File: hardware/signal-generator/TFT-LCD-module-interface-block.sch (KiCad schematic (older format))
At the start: 6 parts, among them J11 SD_Card_Conn, J12 TP_Conn, J13 LCD_Conn, U22 MCP4551-103E/MS

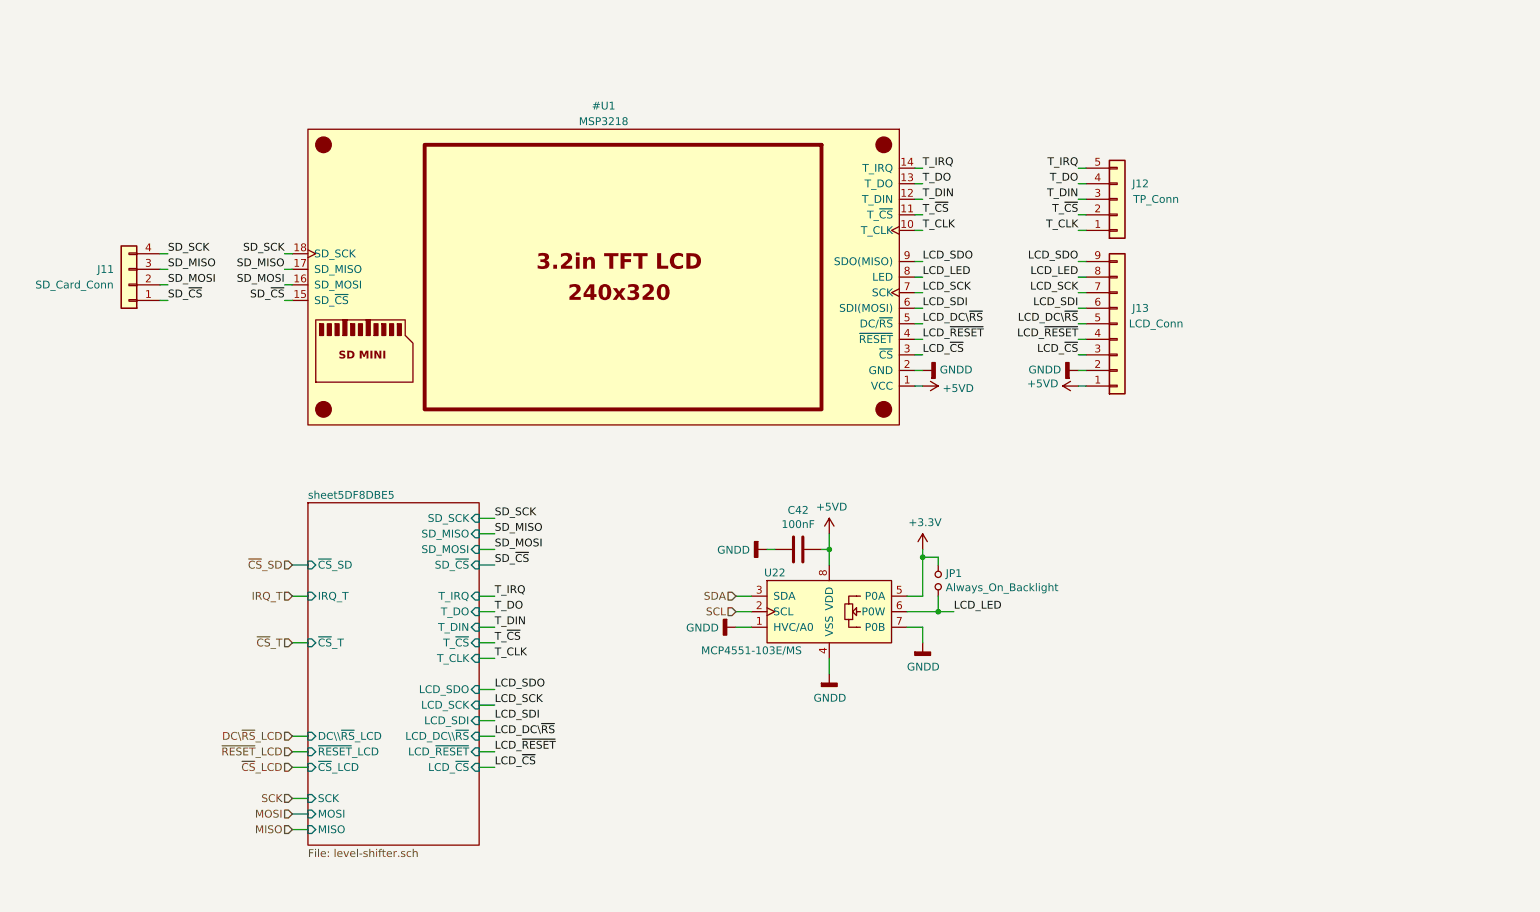
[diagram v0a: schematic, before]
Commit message: [Signal Generator] Change LCD backlight control method
The LCD's backlight was previously intended to be controlled via a
digital potentiometer. However, a much more elegant solution is to
control said backlight via PWM.

Also, removed the level shifter schematic sheet. The level shifters have been
moved to the TFT module's schematic sheet.
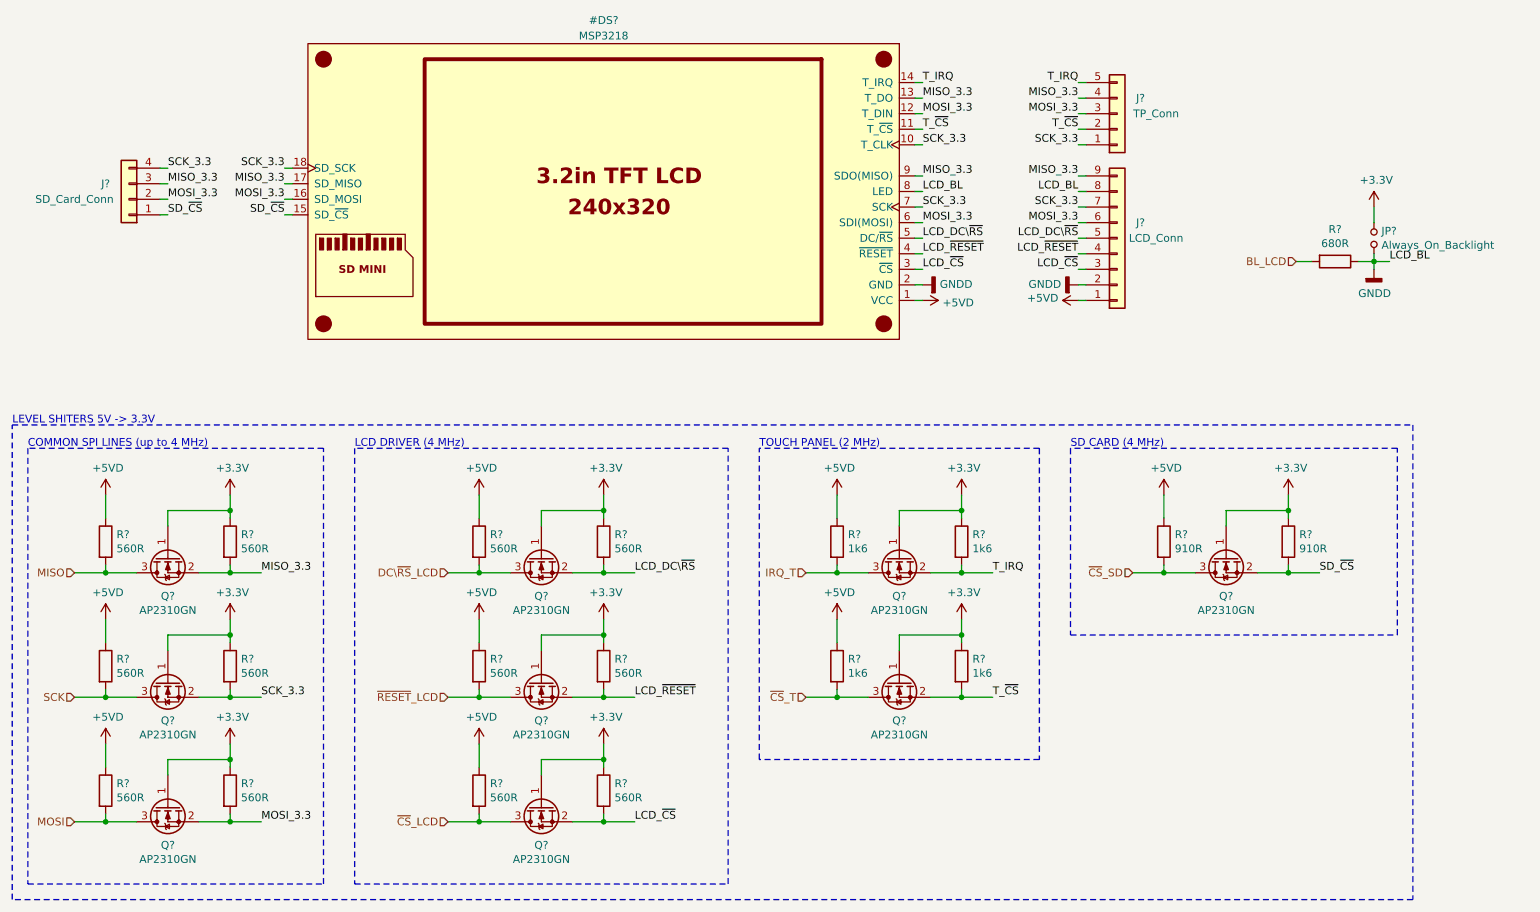
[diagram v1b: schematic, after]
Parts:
- removed C42: 100nF, Capacitors_SMD:C_0805_HandSoldering, symbol Device:C
- removed U22: MCP4551-103E/MS, Housings_SSOP:MSOP-8_3x3mm_Pitch0.65mm, symbol ulib_Digital_Potentiometers:MCP4551-MS
- added Q? (x9): AP2310GN, TO_SOT_Packages_SMD:SOT-23_Handsoldering, symbol ulib_MY_Transistor_FET:AP2310GN
- added R?: 680R, symbol Device:R
- added R? (x2): 910R, Resistors_SMD:R_0805_HandSoldering, symbol Device:R
- added R? (x4): 1k6, Resistors_SMD:R_0805_HandSoldering, symbol Device:R
- added R? (x12): 560R, Resistors_SMD:R_0805_HandSoldering, symbol Device:R
- renumbered J13 to J?, J12 to J?, J11 to J?, JP1 to JP?
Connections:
- net LCD_LED is gone; now on net GNDD: J?.8 (Pin_8), JP?.2
- net SD_MISO is gone; now on net MISO_3.3: J?.3 (Pin_3)
- net SD_MOSI is gone; now on net MOSI_3.3: J?.2 (Pin_2)
- net SD_SCK is gone; now on net SCK_3.3: J?.4 (Pin_4)
- net T_CLK is gone; now on net SCK_3.3: J?.1 (Pin_1)
- net T_DIN is gone; now on net MOSI_3.3: J?.3 (Pin_3)
- net T_DO is gone; now on net MISO_3.3: J?.4 (Pin_4)
- net +3V3: now also Q?.1, Q?.1, Q?.1, Q?.1, Q?.1, Q?.1, Q?.1, Q?.1, Q?.1, R?.1, R?.1, R?.1, R?.1, R?.1, R?.1, R?.1, R?.1, R?.1
- net +5VD: now also R?.1, R?.1, R?.1, R?.1, R?.1, R?.1, R?.1, R?.1, R?.1
- net DC\~RS~_LCD: now also Q?.3, R?.2
- net GNDD: now also R?.1
- net IRQ_T: now also Q?.3, R?.2
- net LCD_DC\~RS: now also Q?.2, R?.2
- net LCD_~CS: now also Q?.2, R?.2
- net LCD_~RESET: now also Q?.2, R?.2
- net MISO: now also Q?.3, R?.2
- net MOSI: now also Q?.3, R?.2
- net SCK: now also Q?.3, R?.2
- net SD_~CS: now also Q?.2, R?.2
- net T_IRQ: now also Q?.2, R?.2
- net T_~CS: now also Q?.2, R?.2
- net ~CS~_LCD: now also Q?.3, R?.2
- net ~CS~_SD: now also Q?.3, R?.2
- net ~CS~_T: now also Q?.3, R?.2
- net ~RESET~_LCD: now also Q?.3, R?.2
- net LCD_SCK renamed SCK_3.3
- net SCK_3.3: now also Q?.2, R?.2
- net LCD_SDI renamed MOSI_3.3
- net MOSI_3.3: now also Q?.2, R?.2
- net LCD_SDO renamed MISO_3.3
- net MISO_3.3: now also Q?.2, R?.2
- new net BL_LCD: R?.2
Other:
- note added: "COMMON SPI LINES (up to 4 MHz)"
- note added: "LCD DRIVER (4 MHz)"
- note added: "LEVEL SHITERS 5V -> 3.3V"
- note added: "SD CARD (4 MHz)"
- note added: "TOUCH PANEL (2 MHz)"
- moved on the sheet: J?, JP?

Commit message: [Signal Generator] Finalize schematic
The electronic schematic is now finalized. All components have been
annotated. Furthermore, all components have an appropriate footprint
associated to them.
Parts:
- R44: renamed from R?; footprint (none) -> Resistors_SMD:R_0805_HandSoldering
- gave numbers to parts that had none: 31

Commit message: [Signal Generator] Restore PCB layout with new symbol annotations
The new components have been loaded in the PCB file.
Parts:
- renumbered JP1 to JP2, Q7 to Q10, Q8 to Q11, Q9 to Q12, Q1 to Q4, Q2 to Q5, Q3 to Q6, Q4 to Q7, Q5 to Q8, Q6 to Q9, R26 to R35, R27 to R36, R28 to R37, R29 to R38, R30 to R39, R31 to R40, R32 to R41, R33 to R42, R34 to R43, R35 to R44, R36 to R45, R37 to R46, R38 to R47, R39 to R48, R40 to R49, R41 to R50, R42 to R51, R43 to R52, R44 to R53

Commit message: [Signal Generator] Layout microcontroller and its peripheral components
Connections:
- net GNDD: no longer J13.8 (Pin_8), JP2.2, R53.1
- new net LCD_BL: J13.8 (Pin_8), JP2.2, R53.1
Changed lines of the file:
@@
 Sheet 5 5
 Title "Digital Function Generator v2 - TFT LCD Module Interface Block"
-Date "2019-12-21"
+Date "2020-01-02"
 Rev "1"
 Comp "Petar Nikolov"
@@
 	10000 2200 10000 2250
 Connection ~ 10000 2250
-Wire Wire Line
-	10000 2250 10000 2300
-$Comp
-L power:GNDD #PWR0152
-U 1 1 5E00F4BB
-P 10000 2300
-F 0 "#PWR0152" H 10000 2050 50  0001 C CNN
-F 1 "GNDD" H 10004 2145 50  0000 C CNN
-F 2 "" H 10000 2300 50  0001 C CNN
-F 3 "" H 10000 2300 50  0001 C CNN
-	1    10000 2300
-	1    0    0    -1
-$EndComp
 $Comp
 L ulib_MY_Transistor_FET:AP2310GN Q?

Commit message: [Signal Generator] Route TFT LCD interface circuitry
This circuitry includes the level shifters as well as the pin headers to
the LCD.
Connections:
- net MISO_3.3: now also J11.2 (Pin_2); no longer J11.3 (Pin_3)
- net MOSI_3.3: now also J11.3 (Pin_3); no longer J11.2 (Pin_2)
- net SCK_3.3: now also J11.1 (Pin_1); no longer J11.4 (Pin_4)
- net SD_~CS: now also J11.4 (Pin_4); no longer J11.1 (Pin_1)
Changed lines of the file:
@@
 Sheet 5 5
 Title "Digital Function Generator v2 - TFT LCD Module Interface Block"
-Date "2020-01-02"
+Date "2020-01-03"
 Rev "1"
 Comp "Petar Nikolov"
@@
 L Connector_Generic:Conn_01x04 J11
 U 1 1 5DFBC023
-P 2000 1850
+P 2000 1750
 F 0 "J11" H 2150 1750 50  0000 C CNN
-F 1 "SD_Card_Conn" H 2350 1850 50  0000 C CNN
-F 2 "Pin_Headers:Pin_Header_Straight_1x04_Pitch2.54mm" H 2000 1850 50  0001 C CNN
-F 3 "~" H 2000 1850 50  0001 C CNN
-	1    2000 1850
-	-1   0    0    1
+F 1 "SD_Card_Conn" H 2350 1650 50  0000 C CNN
+F 2 "Pin_Headers:Pin_Header_Straight_1x04_Pitch2.54mm" H 2000 1750 50  0001 C CNN
+F 3 "~" H 2000 1750 50  0001 C CNN
+	1    2000 1750
+	-1   0    0    -1
 $EndComp
 $Comp
